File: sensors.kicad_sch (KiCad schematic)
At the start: 2 parts, among them U3 BMP581, U4 BNO085

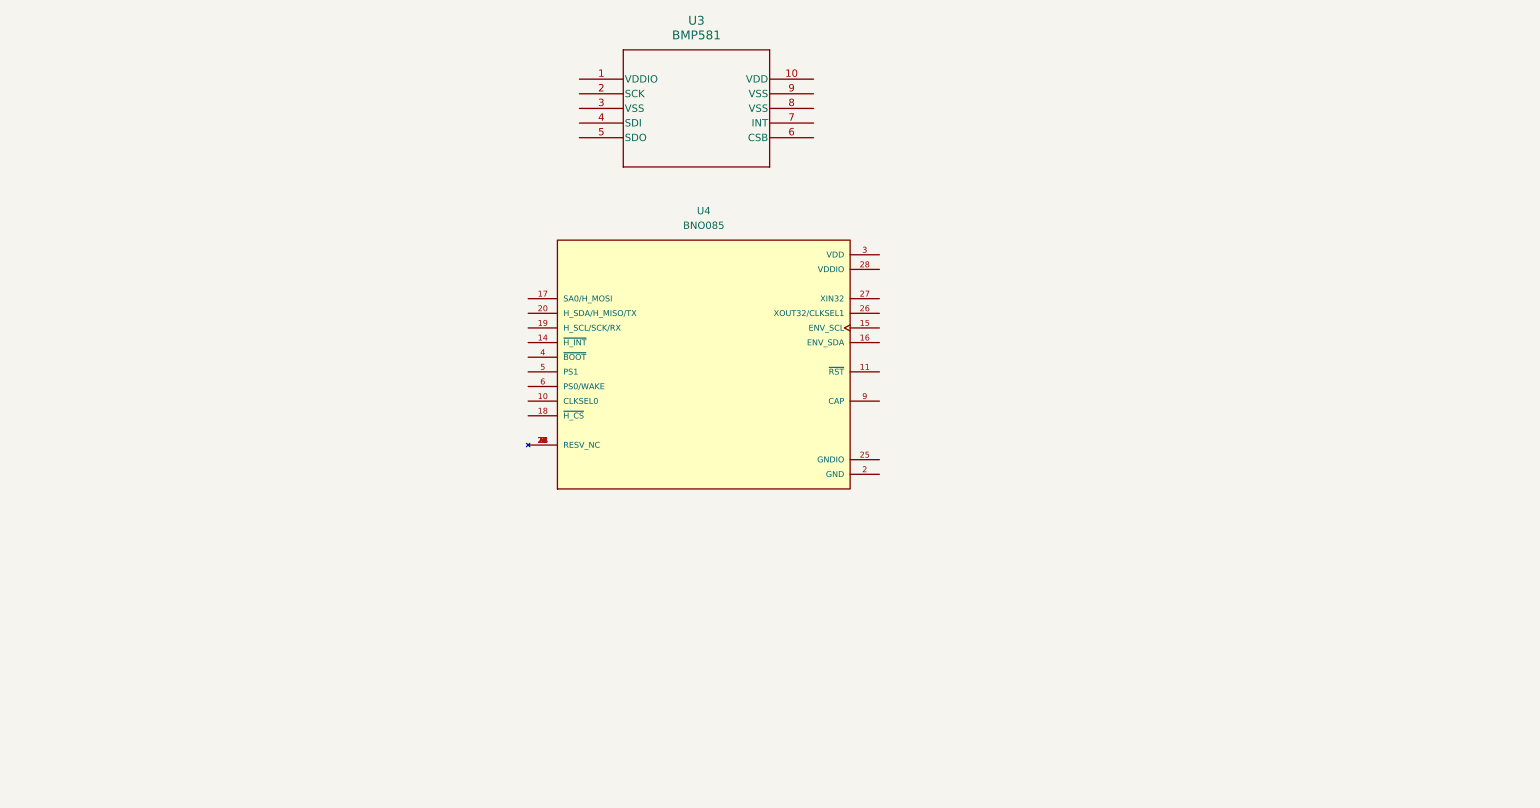
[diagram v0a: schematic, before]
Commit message: Upload architecture diagram, start sensor schematic, add simulation files
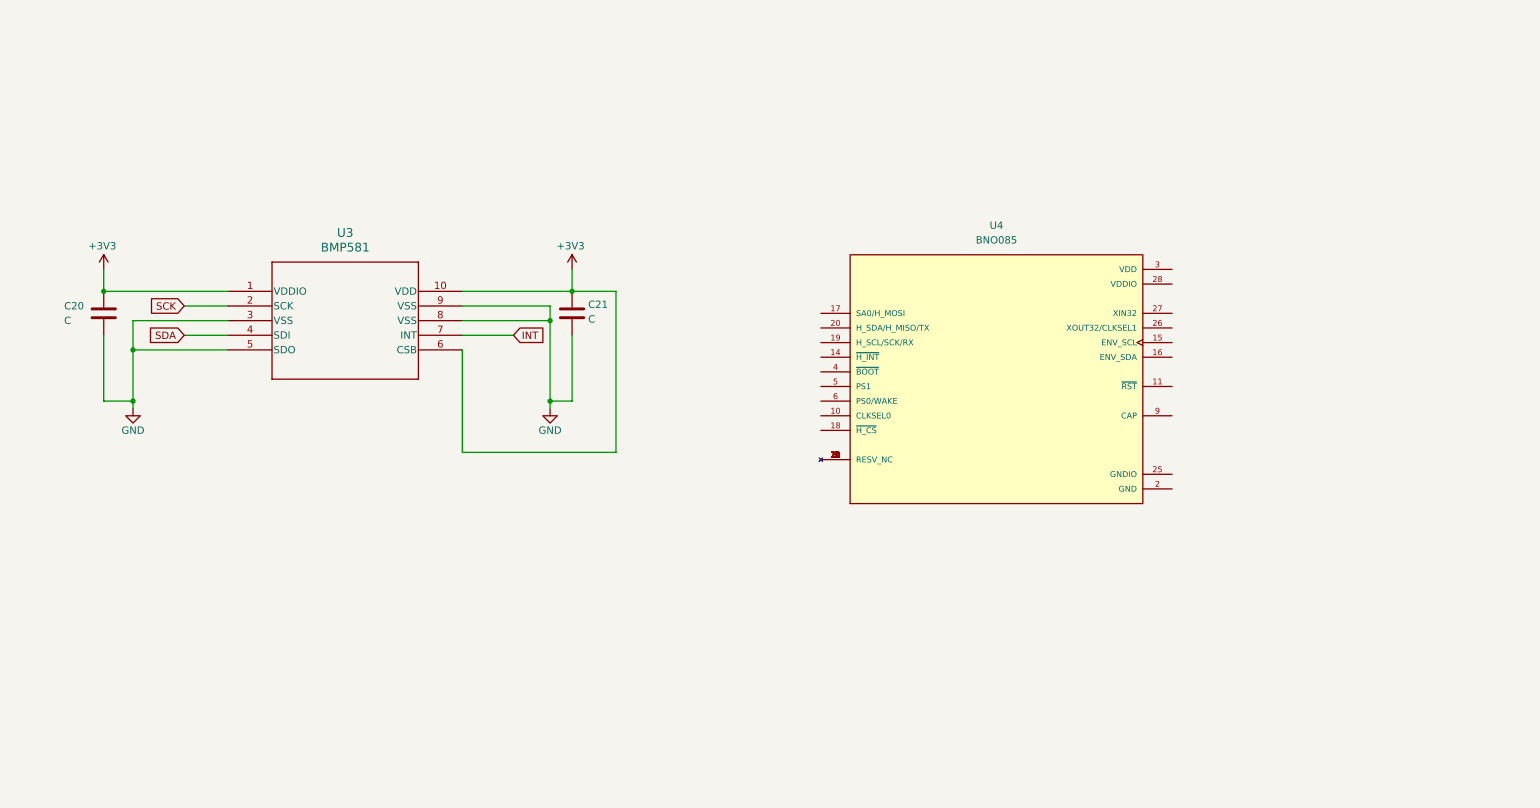
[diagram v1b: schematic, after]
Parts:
- added C20, C21: C, symbol Device:C
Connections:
- net +3V3: now reaches U3.1 (VDDIO)
- net +3V3: now also U3.10 (VDD), U3.6 (CSB), C20.1, C21.1
- net SCK: now reaches U3.2 (SCK)
- net GND: now reaches U3.3 (VSS)
- net GND: now also U3.5 (SDO), U3.8 (VSS), U3.9 (VSS), C20.2, C21.2
- net SDA: now reaches U3.4 (SDI)
- net INT: now reaches U3.7 (INT)
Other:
- moved on the sheet: U3, U4

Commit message: Commit
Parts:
- added C22, C23, C24, C25, C26: C, symbol Device:C
- added R13, R14, R15: R, symbol Device:R
- added Y2: Crystal, symbol Device:Crystal
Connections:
- net +3V3: now also U4.28 (VDDIO), U4.3 (VDD), C22.1, C23.1, R13.1, R14.1, R15.2
- net GND: now also U4.10 (CLKSEL0), U4.17 (SA0/H_MOSI), U4.2 (GND), U4.25 (GNDIO), U4.5 (PS1), U4.6 (PS0/WAKE), C22.2, C23.2, C24.1, C25.2, C26.2
- net SDA: now also U4.20 (H_SDA/H_MISO/TX)
- net RST: now reaches U4.11 (~{RST})
- net HINT: now reaches U4.14 (~{H_INT})
- net at U4.15 (ENV_SCL): now also R14.2
- net at U4.16 (ENV_SDA): now also R13.2
- net SCL: now reaches U4.19 (H_SCL/SCK/RX)
- net at U4.26 (XOUT32/CLKSEL1): now also C25.1, Y2.1
- net at U4.27 (XIN32): now also C26.1, Y2.2
- net at U4.4 (~{BOOT}): now also R15.1
- net at U4.9 (CAP): now also C24.2
- no-connect marks 0 -> 2
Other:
- note added: "Simpler Flight v2"
- title: (none) -> Sensors
- moved on the sheet: C20, C21, U3, U4

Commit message: addecd stuff
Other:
- note added: "Inertial Measurement Unit"
- note added: "Pressure Sensor"
- moved on the sheet: C20, C21, C22, C23, C24, C25, C26, R13, R14, R15, U3, U4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

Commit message: Initiliase main components
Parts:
- C20, C21, C22, C23, C24, C25, C26: footprint (none) -> Capacitor_SMD:C_0805_2012Metric
- R13, R14, R15: footprint (none) -> Resistor_SMD:R_0805_2012Metric_Pad1.20x1.40mm_HandSolder
- U3: footprint footprints:QFN10_BMP581_BOS -> BMP581:QFN10_BMP581_BOS
- Y2: footprint (none) -> Crystal:Crystal_SMD_0603-2Pin_6.0x3.5mm_HandSoldering
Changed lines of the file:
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@@
 			)
 		)
-		(property "Footprint" "footprints:QFN10_BMP581_BOS"
+		(property "Footprint" "BMP581:QFN10_BMP581_BOS"
 			(at 55.88 81.28 0)
 			(effects
@@
 			)
 		)
-		(property "Footprint" ""
+		(property "Footprint" "Capacitor_SMD:C_0805_2012Metric"
 			(at 251.1552 82.55 0)
 			(effects
@@
 			)
 		)
-		(property "Footprint" ""
+		(property "Footprint" "Capacitor_SMD:C_0805_2012Metric"
 			(at 260.0452 107.95 0)
 			(effects
@@
 			)
 		)
-		(property "Footprint" ""
+		(property "Footprint" "Capacitor_SMD:C_0805_2012Metric"
 			(at 239.7252 82.55 0)
 			(effects
@@
 			)
 		)
-		(property "Footprint" ""
+		(property "Footprint" "Resistor_SMD:R_0805_2012Metric_Pad1.20x1.40mm_HandSolder"
 			(at 243.078 105.41 90)
 			(effects
@@
 			)
 		)
-		(property "Footprint" ""
+		(property "Footprint" "Crystal:Crystal_SMD_0603-2Pin_6.0x3.5mm_HandSoldering"
 			(at 264.16 97.79 0)
 			(effects
@@
 			)
 		)
-		(property "Footprint" ""
+		(property "Footprint" "Resistor_SMD:R_0805_2012Metric_Pad1.20x1.40mm_HandSolder"
 			(at 250.698 105.41 90)
 			(effects
@@
 			)
 		)
-		(property "Footprint" ""
+		(property "Footprint" "Capacitor_SMD:C_0805_2012Metric"
 			(at 116.5352 88.9 0)
 			(effects
@@
 			)
 		)
-		(property "Footprint" ""
+		(property "Footprint" "Capacitor_SMD:C_0805_2012Metric"
 			(at 35.2552 88.9 0)
 			(effects
@@
 			)
 		)
-		(property "Footprint" ""
+		(property "Footprint" "Capacitor_SMD:C_0805_2012Metric"
 			(at 270.2052 107.95 0)
 			(effects
@@
 			)
 		)
-		(property "Footprint" ""
+		(property "Footprint" "Capacitor_SMD:C_0805_2012Metric"
 			(at 226.06 112.7252 0)
 			(effects
@@
 			)
 		)
-		(property "Footprint" ""
+		(property "Footprint" "Resistor_SMD:R_0805_2012Metric_Pad1.20x1.40mm_HandSolder"
 			(at 142.748 97.79 90)
 			(effects

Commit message: Updated schematics
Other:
- note added: "CAS Board 2025"
- note removed: "Simpler Flight v2"

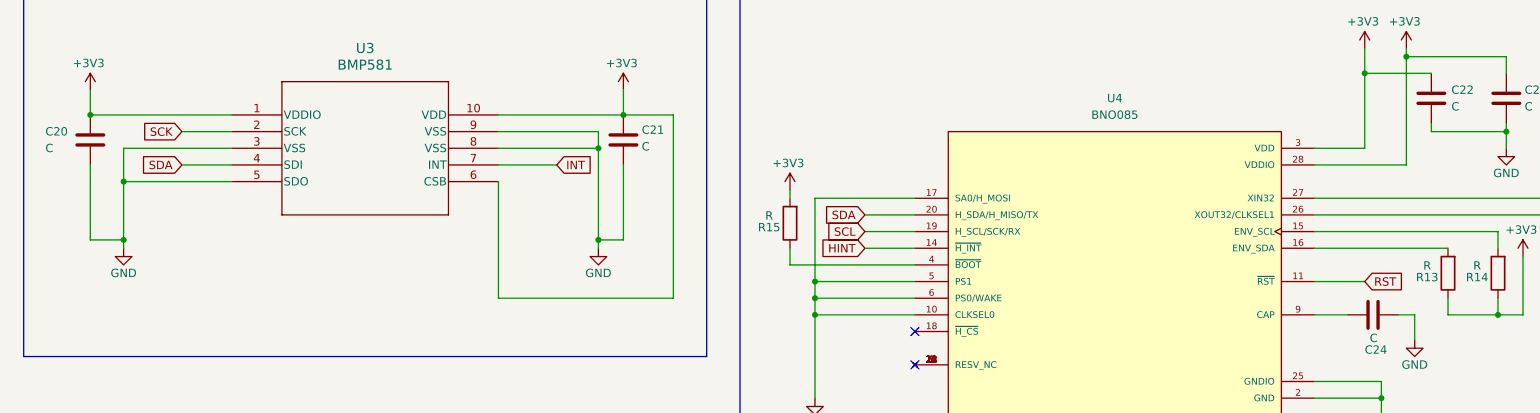
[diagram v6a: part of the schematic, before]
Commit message: Use heirarchical labels
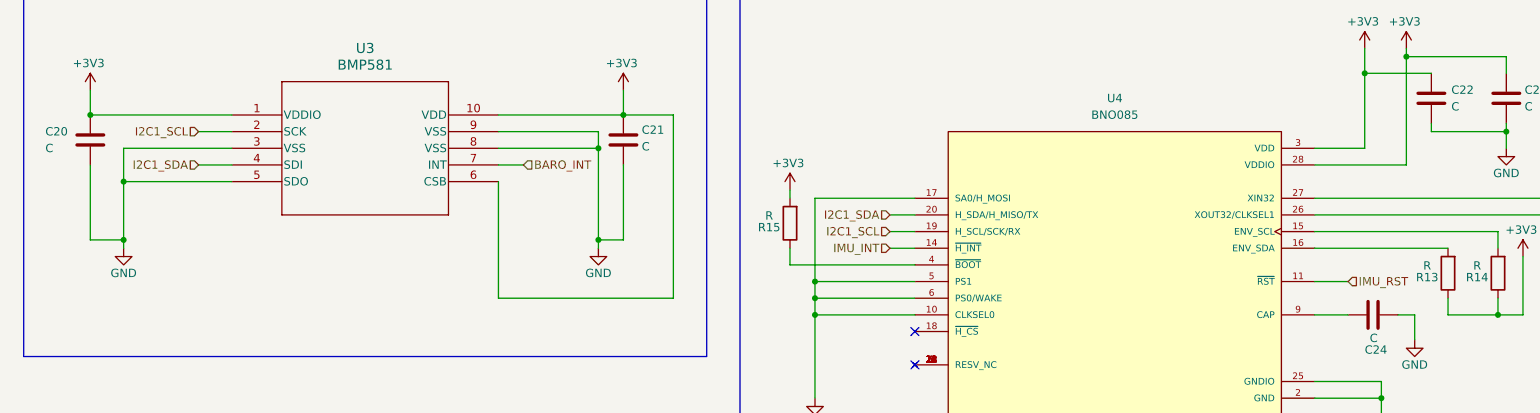
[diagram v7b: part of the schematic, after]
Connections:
- net SCL is gone; now on net I2C1_SCL: U4.19 (H_SCL/SCK/RX)
- net HINT renamed IMU_INT
- net INT renamed BARO_INT
- net RST renamed IMU_RST
- net SCK renamed I2C1_SCL
- net SDA renamed I2C1_SDA
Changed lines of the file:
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@@
 	(wire
 		(pts
-			(xy 48.26 83.82) (xy 55.88 83.82)
+			(xy 50.8 83.82) (xy 55.88 83.82)
 		)
 		(stroke
@@
 	(wire
 		(pts
-			(xy 152.4 101.6) (xy 160.02 101.6)
+			(xy 156.21 101.6) (xy 160.02 101.6)
 		)
 		(stroke
@@
 	(wire
 		(pts
-			(xy 48.26 88.9) (xy 55.88 88.9)
+			(xy 50.8 88.9) (xy 55.88 88.9)
 		)
 		(stroke
@@
 	(wire
 		(pts
-			(xy 34.29 77.47) (xy 34.29 81.28)
+			(xy 96.52 88.9) (xy 100.33 88.9)
 		)
 		(stroke
@@
 	(wire
 		(pts
-			(xy 39.37 86.36) (xy 39.37 91.44)
+			(xy 34.29 77.47) (xy 34.29 81.28)
 		)
 		(stroke
@@
 	(wire
 		(pts
-			(xy 259.08 107.95) (xy 264.16 107.95)
+			(xy 39.37 86.36) (xy 39.37 91.44)
 		)
 		(stroke
@@
 	(wire
 		(pts
-			(xy 233.68 111.76) (xy 236.22 111.76)
+			(xy 259.08 107.95) (xy 264.16 107.95)
 		)
 		(stroke
@@
 	(wire
 		(pts
-			(xy 115.57 88.9) (xy 115.57 100.33)
+			(xy 233.68 111.76) (xy 236.22 111.76)
 		)
 		(stroke
@@
 	(wire
 		(pts
-			(xy 238.76 83.82) (xy 238.76 82.55)
+			(xy 115.57 88.9) (xy 115.57 100.33)
 		)
 		(stroke
@@
 	(wire
 		(pts
-			(xy 144.78 109.22) (xy 160.02 109.22)
+			(xy 238.76 83.82) (xy 238.76 82.55)
 		)
 		(stroke
@@
 	(wire
 		(pts
-			(xy 248.92 109.22) (xy 248.92 111.76)
+			(xy 144.78 109.22) (xy 160.02 109.22)
 		)
 		(stroke
@@
 	(wire
 		(pts
-			(xy 152.4 99.06) (xy 160.02 99.06)
+			(xy 248.92 109.22) (xy 248.92 111.76)
 		)
 		(stroke
@@
 	(wire
 		(pts
-			(xy 220.98 106.68) (xy 228.6 106.68)
+			(xy 220.98 106.68) (xy 226.06 106.68)
 		)
 		(stroke
@@
 	(wire
 		(pts
-			(xy 96.52 88.9) (xy 105.41 88.9)
-		)
-		(stroke
-			(width 0)
-			(type default)
-		)
-	)
-	(wire
-		(pts
 			(xy 160.02 93.98) (xy 144.78 93.98)
 		)
@@
 	(wire
 		(pts
+			(xy 156.21 96.52) (xy 160.02 96.52)
+		)
+		(stroke
+			(width 0)
+			(type default)
+		)
+	)
+	(wire
+		(pts
 			(xy 250.19 72.39) (xy 250.19 74.93)
 		)
@@
 	(wire
 		(pts
-			(xy 55.88 86.36) (xy 39.37 86.36)
+			(xy 156.21 99.06) (xy 160.02 99.06)
 		)
 		(stroke
@@
 	(wire
 		(pts
-			(xy 152.4 96.52) (xy 160.02 96.52)
+			(xy 55.88 86.36) (xy 39.37 86.36)
 		)
 		(stroke
@@
 		)
 	)
-	(global_label "INT"
+	(hierarchical_label "I2C1_SDA"
 		(shape input)
-		(at 105.41 88.9 0)
-		(fields_autoplaced yes)
+		(at 50.8 88.9 180)
 		(effects
 			(font
 				(size 1.27 1.27)
 			)
-			(justify left)
-		)
-		(property "Intersheetrefs" "${INTERSHEET_REFS}"
-			(at 111.2981 88.9 0)
-			(effects
-				(font
-					(size 1.27 1.27)
-				)
-				(justify left)
-			)
+			(justify right)
 		)
 	)
-	(global_label "RST"
+	(hierarchical_label "I2C1_SDA"
 		(shape input)
-		(at 228.6 106.68 0)
-		(fields_autoplaced yes)
+		(at 156.21 96.52 180)
 		(effects
 			(font
 				(size 1.27 1.27)
 			)
-			(justify left)
-		)
-		(property "Intersheetrefs" "${INTERSHEET_REFS}"
-			(at 235.0323 106.68 0)
-			(effects
-				(font
-					(size 1.27 1.27)
-				)
-				(justify left)
-			)
+			(justify right)
 		)
 	)
-	(global_label "HINT"
+	(hierarchical_label "IMU_INT"
 		(shape input)
-		(at 152.4 101.6 180)
-		(fields_autoplaced yes)
+		(at 156.21 101.6 180)
 		(effects
 			(font
@@
 			(justify right)
 		)
-		(property "Intersheetrefs" "${INTERSHEET_REFS}"
-			(at 145.1814 101.6 0)
-			(effects
-				(font
-					(size 1.27 1.27)
-				)
-				(justify right)
-			)
-		)
 	)
-	(global_label "SDA"
+	(hierarchical_label "IMU_RST"
 		(shape input)
-		(at 48.26 88.9 180)
-		(fields_autoplaced yes)
+		(at 226.06 106.68 0)
 		(effects
 			(font
 				(size 1.27 1.27)
 			)
-			(justify right)
-		)
-		(property "Intersheetrefs" "${INTERSHEET_REFS}"
-			(at 41.7067 88.9 0)
-			(effects
-				(font
-					(size 1.27 1.27)
-				)
-				(justify right)
-			)
+			(justify left)
 		)
 	)
-	(global_label "SCL"
+	(hierarchical_label "I2C1_SCL"
 		(shape input)
-		(at 152.4 99.06 180)
-		(fields_autoplaced yes)
+		(at 50.8 83.82 180)
 		(effects
 			(font
@@
 			(justify right)
 		)
-		(property "Intersheetrefs" "${INTERSHEET_REFS}"
-			(at 145.9072 99.06 0)
-			(effects
-				(font
-					(size 1.27 1.27)
-				)
-				(justify right)
-			)
-		)
 	)
-	(global_label "SCK"
+	(hierarchical_label "BARO_INT"
 		(shape input)
-		(at 48.26 83.82 180)
-		(fields_autoplaced yes)
+		(at 100.33 88.9 0)
 		(effects
 			(font
 				(size 1.27 1.27)
 			)
-			(justify right)
-		)
-		(property "Intersheetrefs" "${INTERSHEET_REFS}"
-			(at 41.5253 83.82 0)
-			(effects
-				(font
-					(size 1.27 1.27)
-				)
-				(justify right)
-			)
+			(justify left)
 		)
 	)
-	(global_label "SDA"
+	(hierarchical_label "I2C1_SCL"
 		(shape input)
-		(at 152.4 96.52 180)
-		(fields_autoplaced yes)
+		(at 156.21 99.06 180)
 		(effects
 			(font
@@
 			(justify right)
 		)
-		(property "Intersheetrefs" "${INTERSHEET_REFS}"
-			(at 145.8467 96.52 0)
-			(effects
-				(font
-					(size 1.27 1.27)
-				)
-				(justify right)
-			)
-		)
 	)
